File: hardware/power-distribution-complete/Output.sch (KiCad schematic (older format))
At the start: 88 parts, among them J18 POUT, J19 POUT, J20 POUT, J21 POUT, J22 POUT, J23 POUT, J24 POUT, J25 POUT, J26 POUT, J27 POUT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

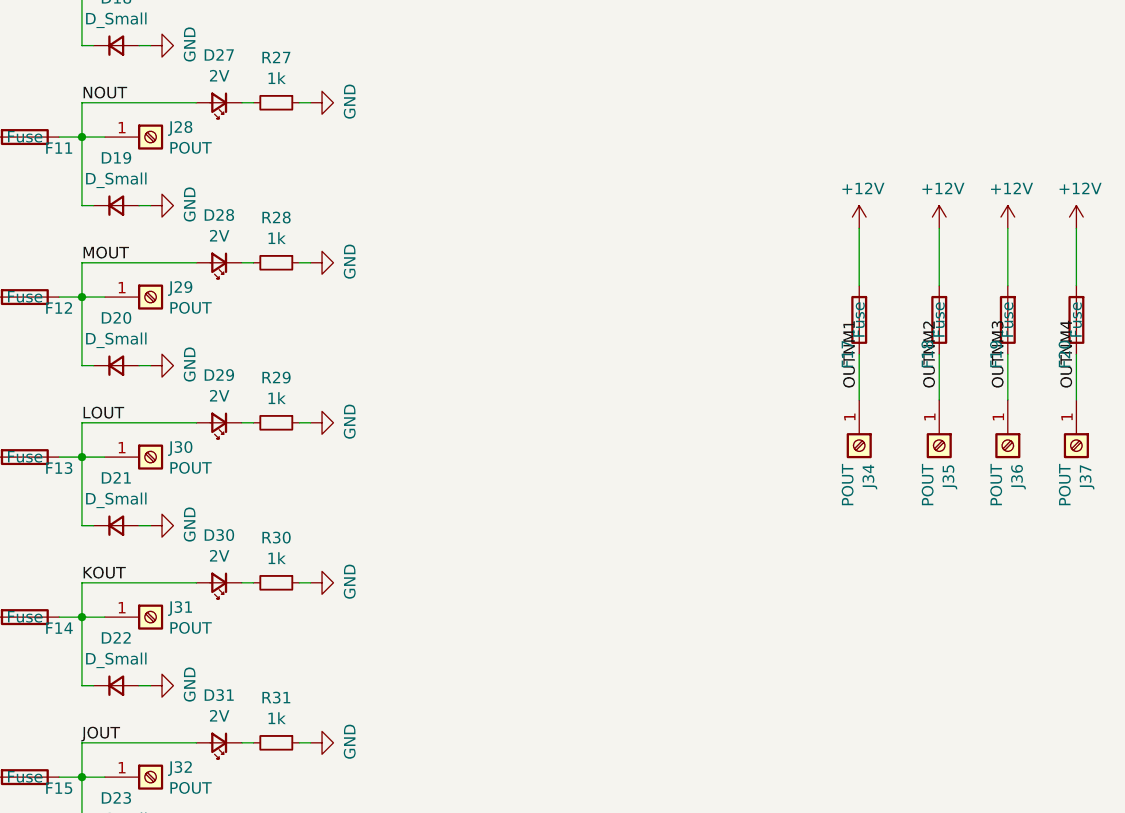
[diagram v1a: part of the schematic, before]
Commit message: Power distribution complete first order
The board is finished and ordered.

Added TVS diode to protect the board from transients.
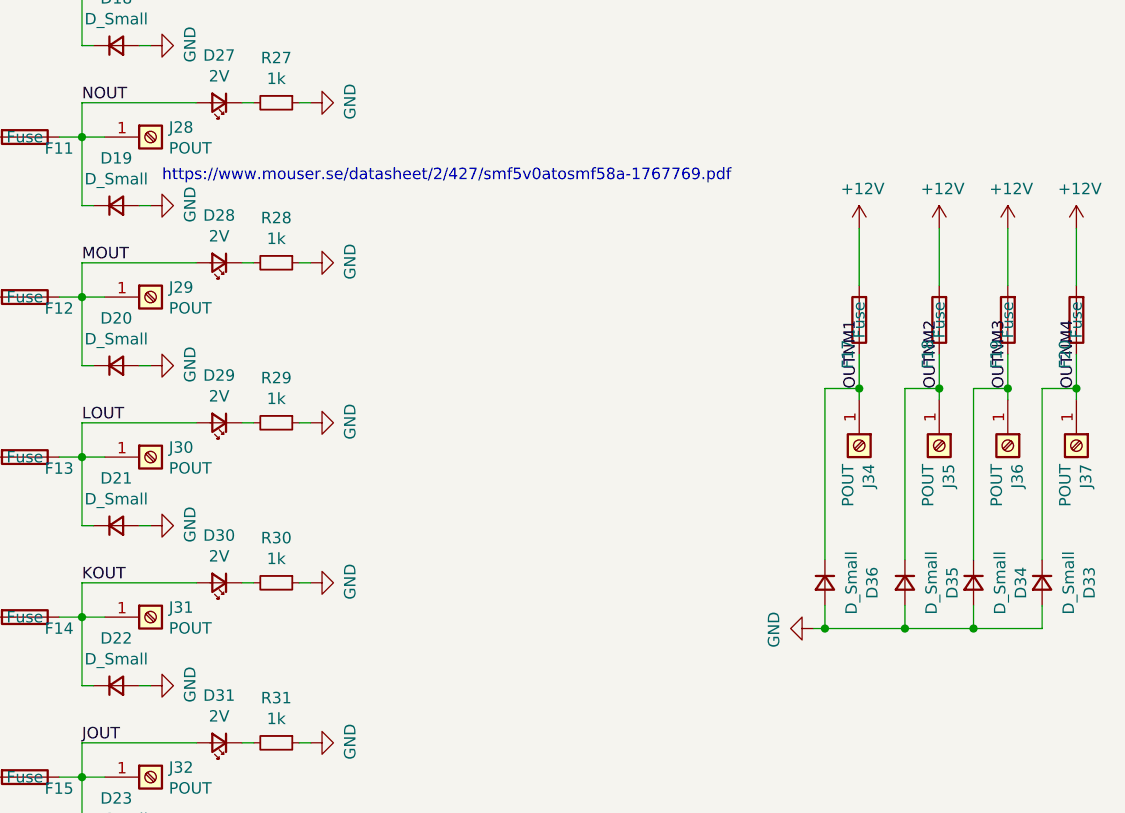
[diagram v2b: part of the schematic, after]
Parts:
- added D33, D34, D35, D36: D_Small, diode:SMF-DO-219AB, symbol Device:D_Small
- D1, D17, D18, D19, D2, D20, D21, D22, D23, D24, D3, D4, D5, D6, D7, D8: footprint diode:SlimSMA_DO-221AC-2 -> diode:SMF-DO-219AB
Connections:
- net GND: now also D33.2 (A), D34.2 (A), D35.2 (A), D36.2 (A)
- net OUTNM1: now also D36.1 (K)
- net OUTNM2: now also D35.1 (K)
- net OUTNM3: now also D34.1 (K)
- net OUTNM4: now also D33.1 (K)
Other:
- note added: "https://www.mouser.se/datasheet/2/427/smf5v0atosmf58a-1767769.pdf"
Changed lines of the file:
@@
 $EndComp
 Wire Wire Line
-	8400 3950 8400 4150
+	8400 3950 8400 4100
 $Comp
 L power:+12V #PWR083
@@
 $EndComp
 Wire Wire Line
-	8750 3950 8750 4150
+	8750 3950 8750 4100
 $Comp
 L power:+12V #PWR084
@@
 $EndComp
 Wire Wire Line
-	9050 3950 9050 4150
+	9050 3950 9050 4100
 $Comp
 L power:+12V #PWR085
@@
 $EndComp
 Wire Wire Line
-	9350 3950 9350 4150
+	9350 3950 9350 4100
 $Comp
 L power:+12V #PWR086
@@
 F 0 "D1" H 2150 2107 50  0000 C CNN
 F 1 "D_Small" H 2150 2016 50  0000 C CNN
-F 2 "diode:SlimSMA_DO-221AC-2" V 2150 1900 50  0001 C CNN
+F 2 "diode:SMF-DO-219AB" V 2150 1900 50  0001 C CNN
 F 3 "~" V 2150 1900 50  0001 C CNN
 	1    2150 1900
@@
 F 0 "D2" H 2150 2807 50  0000 C CNN
 F 1 "D_Small" H 2150 2716 50  0000 C CNN
-F 2 "diode:SlimSMA_DO-221AC-2" V 2150 2600 50  0001 C CNN
+F 2 "diode:SMF-DO-219AB" V 2150 2600 50  0001 C CNN
 F 3 "~" V 2150 2600 50  0001 C CNN
 	1    2150 2600
@@
 F 0 "D3" H 2150 3507 50  0000 C CNN
 F 1 "D_Small" H 2150 3416 50  0000 C CNN
-F 2 "diode:SlimSMA_DO-221AC-2" V 2150 3300 50  0001 C CNN
+F 2 "diode:SMF-DO-219AB" V 2150 3300 50  0001 C CNN
 F 3 "~" V 2150 3300 50  0001 C CNN
 	1    2150 3300
@@
 F 0 "D4" H 2150 4207 50  0000 C CNN
 F 1 "D_Small" H 2150 4116 50  0000 C CNN
-F 2 "diode:SlimSMA_DO-221AC-2" V 2150 4000 50  0001 C CNN
+F 2 "diode:SMF-DO-219AB" V 2150 4000 50  0001 C CNN
 F 3 "~" V 2150 4000 50  0001 C CNN
 	1    2150 4000
@@
 F 0 "D5" H 2150 4907 50  0000 C CNN
 F 1 "D_Small" H 2150 4816 50  0000 C CNN
-F 2 "diode:SlimSMA_DO-221AC-2" V 2150 4700 50  0001 C CNN
+F 2 "diode:SMF-DO-219AB" V 2150 4700 50  0001 C CNN
 F 3 "~" V 2150 4700 50  0001 C CNN
 	1    2150 4700
@@
 F 0 "D6" H 2150 5607 50  0000 C CNN
 F 1 "D_Small" H 2150 5516 50  0000 C CNN
-F 2 "diode:SlimSMA_DO-221AC-2" V 2150 5400 50  0001 C CNN
+F 2 "diode:SMF-DO-219AB" V 2150 5400 50  0001 C CNN
 F 3 "~" V 2150 5400 50  0001 C CNN
 	1    2150 5400
@@
 F 0 "D7" H 2150 6307 50  0000 C CNN
 F 1 "D_Small" H 2150 6216 50  0000 C CNN
-F 2 "diode:SlimSMA_DO-221AC-2" V 2150 6100 50  0001 C CNN
+F 2 "diode:SMF-DO-219AB" V 2150 6100 50  0001 C CNN
 F 3 "~" V 2150 6100 50  0001 C CNN
 	1    2150 6100
@@
 F 0 "D8" H 2150 7007 50  0000 C CNN
 F 1 "D_Small" H 2150 6916 50  0000 C CNN
-F 2 "diode:SlimSMA_DO-221AC-2" V 2150 6800 50  0001 C CNN
+F 2 "diode:SMF-DO-219AB" V 2150 6800 50  0001 C CNN
 F 3 "~" V 2150 6800 50  0001 C CNN
 	1    2150 6800
@@
 F 0 "D24" H 5150 7007 50  0000 C CNN
 F 1 "D_Small" H 5150 6916 50  0000 C CNN
-F 2 "diode:SlimSMA_DO-221AC-2" V 5150 6800 50  0001 C CNN
+F 2 "diode:SMF-DO-219AB" V 5150 6800 50  0001 C CNN
 F 3 "~" V 5150 6800 50  0001 C CNN
 	1    5150 6800
@@
 F 0 "D23" H 5150 6307 50  0000 C CNN
 F 1 "D_Small" H 5150 6216 50  0000 C CNN
-F 2 "diode:SlimSMA_DO-221AC-2" V 5150 6100 50  0001 C CNN
+F 2 "diode:SMF-DO-219AB" V 5150 6100 50  0001 C CNN
 F 3 "~" V 5150 6100 50  0001 C CNN
 	1    5150 6100
@@
 F 0 "D22" H 5150 5607 50  0000 C CNN
 F 1 "D_Small" H 5150 5516 50  0000 C CNN
-F 2 "diode:SlimSMA_DO-221AC-2" V 5150 5400 50  0001 C CNN
+F 2 "diode:SMF-DO-219AB" V 5150 5400 50  0001 C CNN
 F 3 "~" V 5150 5400 50  0001 C CNN
 	1    5150 5400
@@
 F 0 "D21" H 5150 4907 50  0000 C CNN
 F 1 "D_Small" H 5150 4816 50  0000 C CNN
-F 2 "diode:SlimSMA_DO-221AC-2" V 5150 4700 50  0001 C CNN
+F 2 "diode:SMF-DO-219AB" V 5150 4700 50  0001 C CNN
 F 3 "~" V 5150 4700 50  0001 C CNN
 	1    5150 4700
@@
 F 0 "D20" H 5150 4207 50  0000 C CNN
 F 1 "D_Small" H 5150 4116 50  0000 C CNN
-F 2 "diode:SlimSMA_DO-221AC-2" V 5150 4000 50  0001 C CNN
+F 2 "diode:SMF-DO-219AB" V 5150 4000 50  0001 C CNN
 F 3 "~" V 5150 4000 50  0001 C CNN
 	1    5150 4000
@@
 F 0 "D19" H 5150 3507 50  0000 C CNN
 F 1 "D_Small" H 5150 3416 50  0000 C CNN
-F 2 "diode:SlimSMA_DO-221AC-2" V 5150 3300 50  0001 C CNN
+F 2 "diode:SMF-DO-219AB" V 5150 3300 50  0001 C CNN
 F 3 "~" V 5150 3300 50  0001 C CNN
 	1    5150 3300
@@
 F 0 "D18" H 5150 2807 50  0000 C CNN
 F 1 "D_Small" H 5150 2716 50  0000 C CNN
-F 2 "diode:SlimSMA_DO-221AC-2" V 5150 2600 50  0001 C CNN
+F 2 "diode:SMF-DO-219AB" V 5150 2600 50  0001 C CNN
 F 3 "~" V 5150 2600 50  0001 C CNN
 	1    5150 2600
@@
 F 0 "D17" H 5150 2107 50  0000 C CNN
 F 1 "D_Small" H 5150 2016 50  0000 C CNN
-F 2 "diode:SlimSMA_DO-221AC-2" V 5150 1900 50  0001 C CNN
+F 2 "diode:SMF-DO-219AB" V 5150 1900 50  0001 C CNN
 F 3 "~" V 5150 1900 50  0001 C CNN
 	1    5150 1900
@@
 Text Notes 2250 1150 0    50   ~ 0
 150060VS55040
+Text Notes 5350 3200 0    50   ~ 0
+https://www.mouser.se/datasheet/2/427/smf5v0atosmf58a-1767769.pdf
+$Comp
+L Device:D_Small D34
+U 1 1 60131AFE
+P 8900 4950
+F 0 "D34" H 8900 5157 50  0000 C CNN
+F 1 "D_Small" H 8900 5066 50  0000 C CNN
+F 2 "diode:SMF-DO-219AB" V 8900 4950 50  0001 C CNN
+F 3 "~" V 8900 4950 50  0001 C CNN
+	1    8900 4950
+	0    1    1    0
+$EndComp
+$Comp
+L Device:D_Small D35
+U 1 1 60132000
+P 8600 4950
+F 0 "D35" H 8600 5157 50  0000 C CNN
+F 1 "D_Small" H 8600 5066 50  0000 C CNN
+F 2 "diode:SMF-DO-219AB" V 8600 4950 50  0001 C CNN
+F 3 "~" V 8600 4950 50  0001 C CNN
+	1    8600 4950
+	0    1    1    0
+$EndComp
+$Comp
+L Device:D_Small D36
+U 1 1 601324CA
+P 8250 4950
+F 0 "D36" H 8250 5157 50  0000 C CNN
+F 1 "D_Small" H 8250 5066 50  0000 C CNN
+F 2 "diode:SMF-DO-219AB" V 8250 4950 50  0001 C CNN
+F 3 "~" V 8250 4950 50  0001 C CNN
+	1    8250 4950
+	0    1    1    0
+$EndComp
+$Comp
+L Device:D_Small D33
+U 1 1 60132813
+P 9200 4950
+F 0 "D33" H 9200 5157 50  0000 C CNN
+F 1 "D_Small" H 9200 5066 50  0000 C CNN
+F 2 "diode:SMF-DO-219AB" V 9200 4950 50  0001 C CNN
+F 3 "~" V 9200 4950 50  0001 C CNN
+	1    9200 4950
+	0    1    1    0
+$EndComp
+$Comp
+L power:GND #PWR?
+U 1 1 601581EB
+P 8200 5150
+AR Path="/601581EB" Ref="#PWR?"  Part="1"
+AR Path="/5FEC946E/601581EB" Ref="#PWR0106"  Part="1"
+F 0 "#PWR0106" H 8200 4900 50  0001 C CNN
+F 1 "GND" H 8205 4977 50  0000 C CNN
+F 2 "" H 8200 5150 50  0001 C CNN
+F 3 "" H 8200 5150 50  0001 C CNN
+	1    8200 5150
+	0    1    1    0
+$EndComp
+Wire Wire Line
+	8200 5150 8250 5150
+Wire Wire Line
+	9200 5150 9200 5050
+Wire Wire Line
+	8900 5050 8900 5150
+Connection ~ 8900 5150
+Wire Wire Line
+	8900 5150 9200 5150
+Wire Wire Line
+	8600 5050 8600 5150
+Connection ~ 8600 5150
+Wire Wire Line
+	8600 5150 8900 5150
+Wire Wire Line
+	8250 5050 8250 5150
+Connection ~ 8250 5150
+Wire Wire Line
+	8250 5150 8600 5150
+Wire Wire Line
+	8250 4100 8400 4100
+Wire Wire Line
+	8250 4100 8250 4850
+Connection ~ 8400 4100
+Wire Wire Line
+	8400 4100 8400 4150
+Wire Wire Line
+	8600 4100 8750 4100
+Wire Wire Line
+	8600 4100 8600 4850
+Connection ~ 8750 4100
+Wire Wire Line
+	8750 4100 8750 4150
+Wire Wire Line
+	8900 4100 9050 4100
+Wire Wire Line
+	8900 4100 8900 4850
+Connection ~ 9050 4100
+Wire Wire Line
+	9050 4100 9050 4150
+Wire Wire Line
+	9200 4100 9350 4100
+Wire Wire Line
+	9200 4100 9200 4850
+Connection ~ 9350 4100
+Wire Wire Line
+	9350 4100 9350 4150
 $EndSCHEMATC
